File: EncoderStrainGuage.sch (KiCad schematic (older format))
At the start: 58 parts, among them IC1 LM60CIM3_NOPB, J1 Conn_01x05, J2 MM8130-2600RA2, J3 MM8130-2600RA2, J4 Rotary Encoder, J5 Conn_01x02_Male, J6 Conn_01x02_Male, U1 PIC16LF88-I_SO, U2 OPAMP, U3 CC2570RHAT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

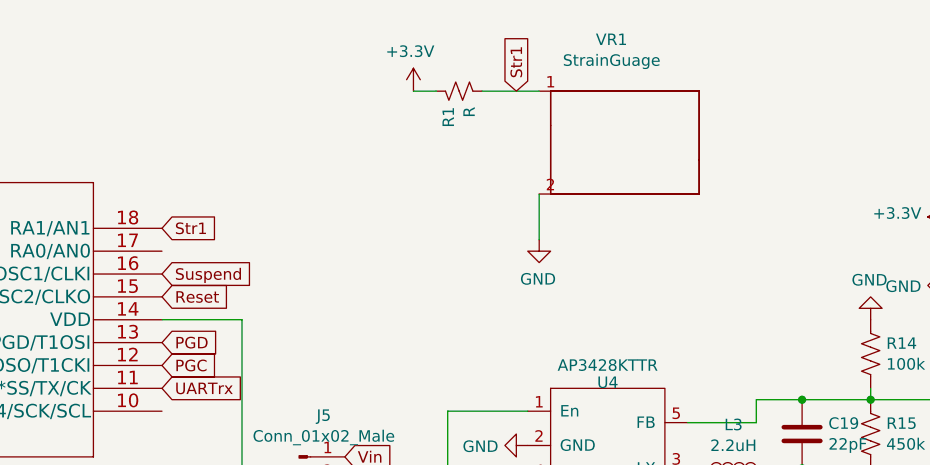
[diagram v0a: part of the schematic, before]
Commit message: Wheatstone Bridge added.
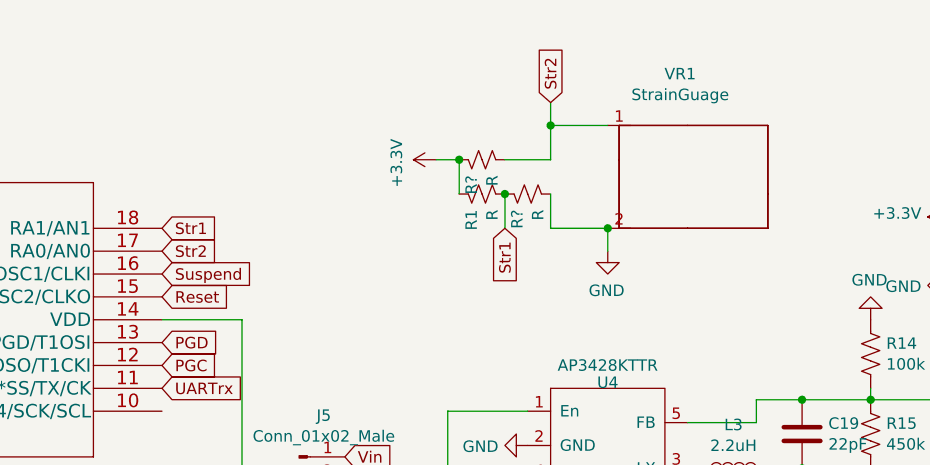
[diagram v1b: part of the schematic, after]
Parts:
- added R? (x2): R, Resistor_SMD:R_0603_1608Metric, symbol EncoderStrainGuage-rescue:R_Small_US-Device
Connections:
- net +3V3: now also R?.1
- net GND: now also R?.2
- net Str1: now also R?.1; no longer VR1.1
- net Str2: now reaches U1.17 (RA0/AN0)
- net Str2: now also VR1.1, R?.2
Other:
- moved on the sheet: R1, VR1
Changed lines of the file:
@@
 EESchema Schematic File Version 4
-LIBS:EncoderStrainGuage-cache
 EELAYER 30 0
 EELAYER END
@@
 Connection ~ 14850 6850
 $Comp
-L EncoderStrainGuage-rescue:GND-power #PWR0105
-U 1 1 5DB86977
-P 9950 1650
-F 0 "#PWR0105" H 9950 1400 50  0001 C CNN
-F 1 "GND" H 9955 1477 50  0000 C CNN
-F 2 "" H 9950 1650 50  0001 C CNN
-F 3 "" H 9950 1650 50  0001 C CNN
-	1    9950 1650
-	-1   0    0    -1
-$EndComp
-$Comp
 L EncoderStrainGuage-rescue:StrainGuage-EncoderBoard VR1
 U 1 1 5DB7B57A
-P 10250 950
-F 0 "VR1" H 10233 1125 50  0000 C CNN
-F 1 "StrainGuage" H 10233 1034 50  0000 C CNN
-F 2 "Connector_PinHeader_1.00mm:PinHeader_1x02_P1.00mm_Vertical" H 10250 950 50  0001 C CNN
-F 3 "" H 10250 950 50  0001 C CNN
-	1    10250 950
+P 10550 1100
+F 0 "VR1" H 10533 1275 50  0000 C CNN
+F 1 "StrainGuage" H 10533 1184 50  0000 C CNN
+F 2 "Connector_PinHeader_1.00mm:PinHeader_1x02_P1.00mm_Vertical" H 10550 1100 50  0001 C CNN
+F 3 "" H 10550 1100 50  0001 C CNN
+	1    10550 1100
 	-1   0    0    -1
 $EndComp
@@
 L EncoderStrainGuage-rescue:+3.3V-power #PWR0104
 U 1 1 5DBA0468
-P 9400 1000
-F 0 "#PWR0104" H 9400 850 50  0001 C CNN
-F 1 "+3.3V" H 9415 1173 50  0000 C CNN
-F 2 "" H 9400 1000 50  0001 C CNN
-F 3 "" H 9400 1000 50  0001 C CNN
-	1    9400 1000
-	-1   0    0    -1
+P 9500 1300
+F 0 "#PWR0104" H 9500 1150 50  0001 C CNN
+F 1 "+3.3V" H 9515 1473 50  0000 C CNN
+F 2 "" H 9500 1300 50  0001 C CNN
+F 3 "" H 9500 1300 50  0001 C CNN
+	1    9500 1300
+	0    -1   1    0
 $EndComp
 $Comp
 L EncoderStrainGuage-rescue:R_Small_US-Device R1
 U 1 1 5DB10D81
-P 9600 1000
-F 0 "R1" H 9668 1046 50  0000 L CNN
-F 1 "R" H 9668 955 50  0000 L CNN
-F 2 "Resistor_SMD:R_0603_1608Metric" H 9600 1000 50  0001 C CNN
-F 3 "~" H 9600 1000 50  0001 C CNN
-	1    9600 1000
+P 9700 1450
+F 0 "R1" H 9768 1496 50  0000 L CNN
+F 1 "R" H 9768 1405 50  0000 L CNN
+F 2 "Resistor_SMD:R_0603_1608Metric" H 9700 1450 50  0001 C CNN
+F 3 "~" H 9700 1450 50  0001 C CNN
+	1    9700 1450
 	0    -1   1    0
 $EndComp
-Wire Wire Line
-	9950 1650 9950 1450
-Text GLabel 9850 1000 1    50   Input ~ 0
+Text GLabel 9800 1600 3    50   Input ~ 0
 Str1
 Wire Wire Line
-	9400 1000 9500 1000
+	9500 1300 9600 1300
 Text GLabel 8300 1600 2    50   Input ~ 0
 Str1
@@
 Text GLabel 3900 1600 0    50   Input ~ 0
 PotOut
-Wire Wire Line
-	9700 1000 9950 1000
 $Comp
 L AP3428KTTR:AP3428KTTR U4
@@
 	1    0    0    -1
 $EndComp
+$Comp
+L EncoderStrainGuage-rescue:R_Small_US-Device R?
+U 1 1 5E33E6F3
+P 9900 1450
+F 0 "R?" H 9968 1496 50  0000 L CNN
+F 1 "R" H 9968 1405 50  0000 L CNN
+F 2 "Resistor_SMD:R_0603_1608Metric" H 9900 1450 50  0001 C CNN
+F 3 "~" H 9900 1450 50  0001 C CNN
+	1    9900 1450
+	0    -1   1    0
+$EndComp
+$Comp
+L EncoderStrainGuage-rescue:R_Small_US-Device R?
+U 1 1 5E33F52D
+P 9700 1300
+F 0 "R?" H 9768 1346 50  0000 L CNN
+F 1 "R" H 9768 1255 50  0000 L CNN
+F 2 "Resistor_SMD:R_0603_1608Metric" H 9700 1300 50  0001 C CNN
+F 3 "~" H 9700 1300 50  0001 C CNN
+	1    9700 1300
+	0    -1   1    0
+$EndComp
+Wire Wire Line
+	9600 1450 9600 1300
+Connection ~ 9600 1300
+Wire Wire Line
+	9800 1600 9800 1450
+Text GLabel 10000 1050 1    50   Input ~ 0
+Str2
+Connection ~ 9800 1450
+Wire Wire Line
+	10000 1450 10000 1600
+Wire Wire Line
+	10000 1600 10250 1600
+Wire Wire Line
+	9800 1300 10000 1300
+Wire Wire Line
+	10000 1300 10000 1150
+Wire Wire Line
+	10000 1150 10250 1150
+Wire Wire Line
+	10000 1150 10000 1050
+Connection ~ 10000 1150
+Text GLabel 8300 1700 2    50   Input ~ 0
+Str2
+$Comp
+L EncoderStrainGuage-rescue:GND-power #PWR0105
+U 1 1 5DB86977
+P 10250 1700
+F 0 "#PWR0105" H 10250 1450 50  0001 C CNN
+F 1 "GND" H 10255 1527 50  0000 C CNN
+F 2 "" H 10250 1700 50  0001 C CNN
+F 3 "" H 10250 1700 50  0001 C CNN
+	1    10250 1700
+	-1   0    0    -1
+$EndComp
+Wire Wire Line
+	10250 1700 10250 1600
+Connection ~ 10250 1600
 $EndSCHEMATC

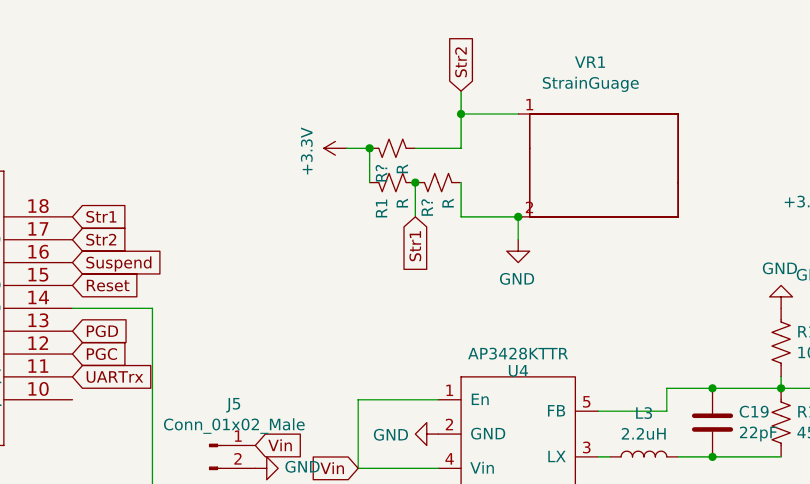
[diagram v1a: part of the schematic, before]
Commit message: routed the wheatstone bridge to the rest of the board
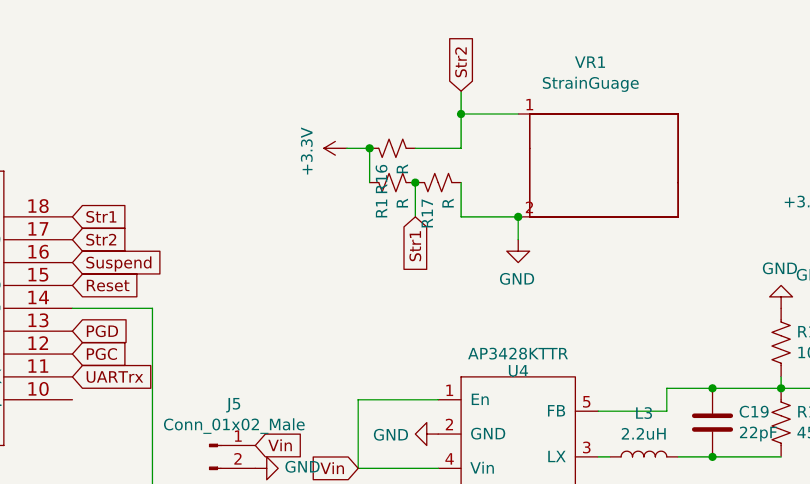
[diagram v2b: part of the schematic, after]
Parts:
- gave numbers to parts that had none: 2
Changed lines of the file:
@@
 EESchema Schematic File Version 4
+LIBS:EncoderStrainGuage-cache
 EELAYER 30 0
 EELAYER END
@@
 $EndComp
 $Comp
-L EncoderStrainGuage-rescue:R_Small_US-Device R?
+L EncoderStrainGuage-rescue:R_Small_US-Device R17
 U 1 1 5E33E6F3
 P 9900 1450
-F 0 "R?" H 9968 1496 50  0000 L CNN
+F 0 "R17" H 9968 1496 50  0000 L CNN
 F 1 "R" H 9968 1405 50  0000 L CNN
 F 2 "Resistor_SMD:R_0603_1608Metric" H 9900 1450 50  0001 C CNN
@@
 $EndComp
 $Comp
-L EncoderStrainGuage-rescue:R_Small_US-Device R?
+L EncoderStrainGuage-rescue:R_Small_US-Device R16
 U 1 1 5E33F52D
 P 9700 1300
-F 0 "R?" H 9768 1346 50  0000 L CNN
+F 0 "R16" H 9768 1346 50  0000 L CNN
 F 1 "R" H 9768 1255 50  0000 L CNN
 F 2 "Resistor_SMD:R_0603_1608Metric" H 9700 1300 50  0001 C CNN

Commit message: added amplifier IC
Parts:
- removed R17: R, Resistor_SMD:R_0603_1608Metric, symbol EncoderStrainGuage-rescue:R_Small_US-Device
- added C21, C22: 100n, Capacitor_SMD:C_0603_1608Metric, symbol EncoderStrainGuage-rescue:C-Device
- added RV1: R_POT_TRIM, symbol Device:R_POT_TRIM_US
- added Rgain1: 500, Resistor_SMD:R_0603_1608Metric, symbol EncoderStrainGuage-rescue:R_US-Device
- added U5: INA333AIDGKR, SOP65P490X110-8N, symbol amplifier_INA333AIDGKR:INA333AIDGKR
- C19, C20: symbol Device:C -> EncoderStrainGuage-rescue:C-Device
- J4: symbol Connector:Conn_01x03_Male -> EncoderStrainGuage-rescue:Conn_01x03_Male-Connector
- J5, J6: symbol Connector:Conn_01x02_Male -> EncoderStrainGuage-rescue:Conn_01x02_Male-Connector
- L3: symbol Device:L -> EncoderStrainGuage-rescue:L-Device
- R14, R15: symbol Device:R_US -> EncoderStrainGuage-rescue:R_US-Device
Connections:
- net +3V3: now also C21.1, U5.7 (V+)
- net GND: now also C21.2, C22.1, C22.2, RV1.1, U5.4 (V-)
- net Str1: now also U5.6 (VOUT); no longer R1.2
- net Str2: now also U5.5 (REF); no longer R16.2, VR1.1
- new net: Rgain1.2, U5.1 (RG)
- new net: Rgain1.1, U5.8 (RG_2)
- new net Str+: R16.2, U5.2 (VIN-), VR1.1
- new net Str-: R1.2, RV1.3, U5.3 (VIN+)
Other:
- moved on the sheet: R1, R16
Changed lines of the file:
@@
 EESchema Schematic File Version 4
-LIBS:EncoderStrainGuage-cache
 EELAYER 30 0
 EELAYER END
@@
 L EncoderStrainGuage-rescue:+3.3V-power #PWR0104
 U 1 1 5DBA0468
-P 9500 1300
-F 0 "#PWR0104" H 9500 1150 50  0001 C CNN
-F 1 "+3.3V" H 9515 1473 50  0000 C CNN
-F 2 "" H 9500 1300 50  0001 C CNN
-F 3 "" H 9500 1300 50  0001 C CNN
-	1    9500 1300
+P 9250 1300
+F 0 "#PWR0104" H 9250 1150 50  0001 C CNN
+F 1 "+3.3V" H 9265 1473 50  0000 C CNN
+F 2 "" H 9250 1300 50  0001 C CNN
+F 3 "" H 9250 1300 50  0001 C CNN
+	1    9250 1300
 	0    -1   1    0
 $EndComp
@@
 L EncoderStrainGuage-rescue:R_Small_US-Device R1
 U 1 1 5DB10D81
-P 9700 1450
-F 0 "R1" H 9768 1496 50  0000 L CNN
-F 1 "R" H 9768 1405 50  0000 L CNN
-F 2 "Resistor_SMD:R_0603_1608Metric" H 9700 1450 50  0001 C CNN
-F 3 "~" H 9700 1450 50  0001 C CNN
-	1    9700 1450
+P 9450 1600
+F 0 "R1" H 9518 1646 50  0000 L CNN
+F 1 "R" H 9518 1555 50  0000 L CNN
+F 2 "Resistor_SMD:R_0603_1608Metric" H 9450 1600 50  0001 C CNN
+F 3 "~" H 9450 1600 50  0001 C CNN
+	1    9450 1600
 	0    -1   1    0
 $EndComp
-Text GLabel 9800 1600 3    50   Input ~ 0
-Str1
-Wire Wire Line
-	9500 1300 9600 1300
+Wire Wire Line
+	9250 1300 9350 1300
 Text GLabel 8300 1600 2    50   Input ~ 0
 Str1
@@
 XOSC1
 $Comp
-L Connector:Conn_01x03_Male J4
+L EncoderStrainGuage-rescue:Conn_01x03_Male-Connector J4
 U 1 1 5E2DD770
 P 10050 3000
@@
 $EndComp
 $Comp
-L power:GND #PWR0101
+L EncoderStrainGuage-rescue:GND-power #PWR0101
 U 1 1 5E460A71
 P 9850 3100
@@
 $EndComp
 $Comp
-L power:+3.3V #PWR0113
+L EncoderStrainGuage-rescue:+3.3V-power #PWR0113
 U 1 1 5E46154F
 P 9850 2900
@@
 $EndComp
 $Comp
-L power:GND #PWR0161
+L EncoderStrainGuage-rescue:GND-power #PWR0161
 U 1 1 5E4693A7
 P 9900 2550
@@
 $EndComp
 $Comp
-L Device:L L3
+L EncoderStrainGuage-rescue:L-Device L3
 U 1 1 5E4694B5
 P 10800 2650
@@
 $EndComp
 $Comp
-L Device:C C19
+L EncoderStrainGuage-rescue:C-Device C19
 U 1 1 5E46B3FE
 P 11100 2500
@@
 $EndComp
 $Comp
-L Device:R_US R15
+L EncoderStrainGuage-rescue:R_US-Device R15
 U 1 1 5E46CE46
 P 11400 2500
@@
 $EndComp
 $Comp
-L Device:R_US R14
+L EncoderStrainGuage-rescue:R_US-Device R14
 U 1 1 5E46DAD4
 P 11400 2150
@@
 $EndComp
 $Comp
-L Device:C C20
+L EncoderStrainGuage-rescue:C-Device C20
 U 1 1 5E46E6DD
 P 11750 2500
@@
 	11400 2350 11750 2350
 $Comp
-L power:GND #PWR0162
+L EncoderStrainGuage-rescue:GND-power #PWR0162
 U 1 1 5E486368
 P 11750 2650
@@
 $EndComp
 $Comp
-L power:GND #PWR0163
+L EncoderStrainGuage-rescue:GND-power #PWR0163
 U 1 1 5E486735
 P 11400 2000
@@
 Vin
 $Comp
-L power:+3.3V #PWR0164
+L EncoderStrainGuage-rescue:+3.3V-power #PWR0164
 U 1 1 5E48BE43
 P 11750 2350
@@
 Connection ~ 11750 2350
 $Comp
-L Connector:Conn_01x02_Male J5
+L EncoderStrainGuage-rescue:Conn_01x02_Male-Connector J5
 U 1 1 5E48D248
 P 8900 2600
@@
 Vin
 $Comp
-L power:GND #PWR0165
+L EncoderStrainGuage-rescue:GND-power #PWR0165
 U 1 1 5E48EB98
 P 9100 2700
@@
 	13650 3250 13850 3250
 $Comp
-L Connector:Conn_01x02_Male J6
+L EncoderStrainGuage-rescue:Conn_01x02_Male-Connector J6
 U 1 1 5E551962
 P 5400 6950
@@
 	5600 6450 5600 6950
 $Comp
-L power:+3.3V #PWR0111
+L EncoderStrainGuage-rescue:+3.3V-power #PWR0111
 U 1 1 5E5B2101
 P 6500 6250
@@
 $EndComp
 $Comp
-L EncoderStrainGuage-rescue:R_Small_US-Device R17
-U 1 1 5E33E6F3
-P 9900 1450
-F 0 "R17" H 9968 1496 50  0000 L CNN
-F 1 "R" H 9968 1405 50  0000 L CNN
-F 2 "Resistor_SMD:R_0603_1608Metric" H 9900 1450 50  0001 C CNN
-F 3 "~" H 9900 1450 50  0001 C CNN
-	1    9900 1450
-	0    -1   1    0
-$EndComp
-$Comp
 L EncoderStrainGuage-rescue:R_Small_US-Device R16
 U 1 1 5E33F52D
-P 9700 1300
-F 0 "R16" H 9768 1346 50  0000 L CNN
-F 1 "R" H 9768 1255 50  0000 L CNN
-F 2 "Resistor_SMD:R_0603_1608Metric" H 9700 1300 50  0001 C CNN
-F 3 "~" H 9700 1300 50  0001 C CNN
-	1    9700 1300
+P 9450 1300
+F 0 "R16" H 9518 1346 50  0000 L CNN
+F 1 "R" H 9518 1255 50  0000 L CNN
+F 2 "Resistor_SMD:R_0603_1608Metric" H 9450 1300 50  0001 C CNN
+F 3 "~" H 9450 1300 50  0001 C CNN
+	1    9450 1300
 	0    -1   1    0
 $EndComp
-Wire Wire Line
-	9600 1450 9600 1300
-Connection ~ 9600 1300
-Wire Wire Line
-	9800 1600 9800 1450
 Text GLabel 10000 1050 1    50   Input ~ 0
-Str2
-Connection ~ 9800 1450
-Wire Wire Line
-	10000 1450 10000 1600
+Str+
 Wire Wire Line
 	10000 1600 10250 1600
-Wire Wire Line
-	9800 1300 10000 1300
 Wire Wire Line
 	10000 1300 10000 1150
@@
 	10250 1700 10250 1600
 Connection ~ 10250 1600
+Text GLabel 15250 1200 2    50   Input ~ 0
+Str1
+$Comp
+L Device:R_POT_TRIM_US RV1
+U 1 1 5E3FA865
+P 9850 1600
+F 0 "RV1" V 9645 1600 50  0000 C CNN
+F 1 "R_POT_TRIM" V 9736 1600 50  0000 C CNN
+F 2 "" H 9850 1600 50  0001 C CNN
+F 3 "~" H 9850 1600 50  0001 C CNN
+	1    9850 1600
+	0    1    1    0
+$EndComp
+Wire Wire Line
+	9550 1300 10000 1300
+Wire Wire Line
+	9350 1300 9350 1600
+Connection ~ 9350 1300
+Text GLabel 9650 1800 3    50   Input ~ 0
+Str-
+Wire Wire Line
+	9550 1600 9650 1600
+Wire Wire Line
+	9650 1800 9650 1600
+Connection ~ 9650 1600
+Wire Wire Line
+	9650 1600 9700 1600
+Text GLabel 15250 1000 2    50   Input ~ 0
+Str2
+Text GLabel 13850 1500 0    50   Input ~ 0
+Str+
+Text GLabel 13850 1600 0    50   Input ~ 0
+Str-
+Wire Wire Line
+	13550 1300 13550 1200
+Wire Wire Line
+	13550 1200 13850 1200
+$Comp
+L EncoderStrainGuage-rescue:GND-power #PWR02
+U 1 1 5E45E74C
+P 13850 2150
+F 0 "#PWR02" H 13850 1900 50  0001 C CNN
+F 1 "GND" H 13855 1977 50  0000 C CNN
+F 2 "" H 13850 2150 50  0001 C CNN
+F 3 "" H 13850 2150 50  0001 C CNN
+	1    13850 2150
+	-1   0    0    -1
+$EndComp
+$Comp
+L EncoderStrainGuage-rescue:C-Device C22
+U 1 1 5E4FE3E3
+P 13700 2000
+F 0 "C22" H 13815 2046 50  0000 L CNN
+F 1 "100n" H 13815 1955 50  0000 L CNN
+F 2 "Capacitor_SMD:C_0603_1608Metric" H 13738 1850 50  0001 C CNN
+F 3 "~" H 13700 2000 50  0001 C CNN
+	1    13700 2000
+	0    -1   -1   0
+$EndComp
+Wire Wire Line
+	13850 1800 13850 2000
+Connection ~ 13850 2000
+Wire Wire Line
+	13850 2000 13850 2150
+$Comp
+L EncoderStrainGuage-rescue:GND-power #PWR?
+U 1 1 5E55E711
+P 13550 2000
+F 0 "#PWR?" H 13550 1750 50  0001 C CNN
+F 1 "GND" H 13555 1827 50  0000 C CNN
+F 2 "" H 13550 2000 50  0001 C CNN
+F 3 "" H 13550 2000 50  0001 C CNN
+	1    13550 2000
+	-1   0    0    -1
+$EndComp
+$Comp
+L amplifier_INA333AIDGKR:INA333AIDGKR U5
+U 1 1 5E3EBED4
+P 14550 1300
+F 0 "U5" H 14550 1970 50  0000 C CNN
+F 1 "INA333AIDGKR" H 14550 1879 50  0000 C CNN
+F 2 "SOP65P490X110-8N" H 14550 1300 50  0001 L BNN
+F 3 "1631194" H 14550 1300 50  0001 L BNN
+F 4 "01P0907" H 14550 1300 50  0001 L BNN "Field4"
+F 5 "INA333AIDGKR" H 14550 1300 50  0001 L BNN "Field5"
+F 6 "MSOP-8" H 14550 1300 50  0001 L BNN "Field6"
+F 7 "Texas Instruments" H 14550 1300 50  0001 L BNN "Field7"
+	1    14550 1300
+	1    0    0    -1
+$EndComp
+$Comp
+L EncoderStrainGuage-rescue:GND-power #PWR?
+U 1 1 5E56DA51
+P 13400 700
+F 0 "#PWR?" H 13400 450 50  0001 C CNN
+F 1 "GND" H 13405 527 50  0000 C CNN
+F 2 "" H 13400 700 50  0001 C CNN
+F 3 "" H 13400 700 50  0001 C CNN
+	1    13400 700
+	0    -1   1    0
+$EndComp
+Connection ~ 13400 1000
+Wire Wire Line
+	13400 1000 13850 1000
+Wire Wire Line
+	13150 1000 13400 1000
+$Comp
+L EncoderStrainGuage-rescue:C-Device C21
+U 1 1 5E4B0832
+P 13400 850
+F 0 "C21" H 13515 896 50  0000 L CNN
+F 1 "100n" H 13515 805 50  0000 L CNN
+F 2 "Capacitor_SMD:C_0603_1608Metric" H 13438 700 50  0001 C CNN
+F 3 "~" H 13400 850 50  0001 C CNN
+	1    13400 850
+	-1   0    0    1
+$EndComp
+$Comp
+L EncoderStrainGuage-rescue:+3.3V-power #PWR01
+U 1 1 5E463587
+P 13150 1000
+F 0 "#PWR01" H 13150 850 50  0001 C CNN
+F 1 "+3.3V" H 13165 1173 50  0000 C CNN
+F 2 "" H 13150 1000 50  0001 C CNN
+F 3 "" H 13150 1000 50  0001 C CNN
+	1    13150 1000
+	0    -1   1    0
+$EndComp
+$Comp
+L EncoderStrainGuage-rescue:R_US-Device Rgain1
+U 1 1 5E46DCF9
+P 13700 1300
+F 0 "Rgain1" H 13768 1346 50  0000 L CNN
+F 1 "500" H 13768 1255 50  0000 L CNN
+F 2 "Resistor_SMD:R_0603_1608Metric" V 13740 1290 50  0001 C CNN
+F 3 "~" H 13700 1300 50  0001 C CNN
+	1    13700 1300
+	0    -1   -1   0
+$EndComp
 $EndSCHEMATC

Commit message: temp sense caps + amplifier IC
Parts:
- added C23: .1uF, Capacitor_SMD:C_0603_1608Metric, symbol EncoderStrainGuage-rescue:C-Device
- added C24: 1uF, Capacitor_SMD:C_0603_1608Metric, symbol EncoderStrainGuage-rescue:C-Device
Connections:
- net +3V3: now also C23.1
- net GND: now also U5.5 (REF), C23.2, C24.2
- net TempOut: now also C24.1
- net Str2: no longer names the net of U1.17 (RA0/AN0)
- net Str2: no longer U5.5 (REF)
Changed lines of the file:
@@
 	1    0    0    -1
 $EndComp
-Text GLabel 12650 3350 0    50   Input ~ 0
+Text GLabel 12550 3350 0    50   Input ~ 0
 TempOut
 Wire Wire Line
@@
 L EncoderStrainGuage-rescue:+3.3V-power #PWR0102
 U 1 1 5E2C8163
-P 12650 3250
-F 0 "#PWR0102" H 12650 3100 50  0001 C CNN
-F 1 "+3.3V" H 12665 3423 50  0000 C CNN
-F 2 "" H 12650 3250 50  0001 C CNN
-F 3 "" H 12650 3250 50  0001 C CNN
-	1    12650 3250
+P 12550 3250
+F 0 "#PWR0102" H 12550 3100 50  0001 C CNN
+F 1 "+3.3V" H 12565 3423 50  0000 C CNN
+F 2 "" H 12550 3250 50  0001 C CNN
+F 3 "" H 12550 3250 50  0001 C CNN
+	1    12550 3250
 	0    -1   -1   0
 $EndComp
@@
 	10000 1150 10000 1050
 Connection ~ 10000 1150
-Text GLabel 8300 1700 2    50   Input ~ 0
-Str2
 $Comp
 L EncoderStrainGuage-rescue:GND-power #PWR0105
@@
 Wire Wire Line
 	9650 1600 9700 1600
-Text GLabel 15250 1000 2    50   Input ~ 0
-Str2
 Text GLabel 13850 1500 0    50   Input ~ 0
 Str+
@@
 	13850 2000 13850 2150
 $Comp
-L EncoderStrainGuage-rescue:GND-power #PWR?
+L EncoderStrainGuage-rescue:GND-power #PWR06
 U 1 1 5E55E711
 P 13550 2000
-F 0 "#PWR?" H 13550 1750 50  0001 C CNN
+F 0 "#PWR06" H 13550 1750 50  0001 C CNN
 F 1 "GND" H 13555 1827 50  0000 C CNN
 F 2 "" H 13550 2000 50  0001 C CNN
@@
 $EndComp
 $Comp
-L EncoderStrainGuage-rescue:GND-power #PWR?
+L EncoderStrainGuage-rescue:GND-power #PWR05
 U 1 1 5E56DA51
 P 13400 700
-F 0 "#PWR?" H 13400 450 50  0001 C CNN
+F 0 "#PWR05" H 13400 450 50  0001 C CNN
 F 1 "GND" H 13405 527 50  0000 C CNN
 F 2 "" H 13400 700 50  0001 C CNN
@@
 	0    -1   -1   0
 $EndComp
+$Comp
+L power:GND #PWR07
+U 1 1 5E3FA48A
+P 15250 1000
+F 0 "#PWR07" H 15250 750 50  0001 C CNN
+F 1 "GND" H 15255 827 50  0000 C CNN
+F 2 "" H 15250 1000 50  0001 C CNN
+F 3 "" H 15250 1000 50  0001 C CNN
+	1    15250 1000
+	0    -1   -1   0
+$EndComp
+$Comp
+L EncoderStrainGuage-rescue:C-Device C24
+U 1 1 5E412910
+P 12650 3500
+F 0 "C24" H 12765 3546 50  0000 L CNN
+F 1 "1uF" H 12765 3455 50  0000 L CNN
+F 2 "Capacitor_SMD:C_0603_1608Metric" H 12688 3350 50  0001 C CNN
+F 3 "~" H 12650 3500 50  0001 C CNN
+	1    12650 3500
+	1    0    0    -1
+$EndComp
+$Comp
+L EncoderStrainGuage-rescue:GND-power #PWR04
+U 1 1 5E412916
+P 12650 3650
+F 0 "#PWR04" H 12650 3400 50  0001 C CNN
+F 1 "GND" H 12655 3477 50  0000 C CNN
+F 2 "" H 12650 3650 50  0001 C CNN
+F 3 "" H 12650 3650 50  0001 C CNN
+	1    12650 3650
+	1    0    0    -1
+$EndComp
+Wire Wire Line
+	12550 3350 12650 3350
+Connection ~ 12650 3350
+$Comp
+L EncoderStrainGuage-rescue:C-Device C23
+U 1 1 5E42658E
+P 12600 3100
+F 0 "C23" H 12715 3146 50  0000 L CNN
+F 1 ".1uF" H 12715 3055 50  0000 L CNN
+F 2 "Capacitor_SMD:C_0603_1608Metric" H 12638 2950 50  0001 C CNN
+F 3 "~" H 12600 3100 50  0001 C CNN
+	1    12600 3100
+	-1   0    0    1
+$EndComp
+$Comp
+L EncoderStrainGuage-rescue:GND-power #PWR03
+U 1 1 5E426598
+P 12600 2950
+F 0 "#PWR03" H 12600 2700 50  0001 C CNN
+F 1 "GND" H 12605 2777 50  0000 C CNN
+F 2 "" H 12600 2950 50  0001 C CNN
+F 3 "" H 12600 2950 50  0001 C CNN
+	1    12600 2950
+	-1   0    0    1
+$EndComp
+Wire Wire Line
+	12550 3250 12600 3250
+Connection ~ 12600 3250
+Wire Wire Line
+	12600 3250 12650 3250
 $EndSCHEMATC
